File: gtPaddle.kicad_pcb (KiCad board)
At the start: 2 copper layers, 60.6 x 72.6 mm, 46 parts, among them IC1 74157N, IC2 74157N, J1 Conn_01x02_Pin, J2 Conn_01x02_Pin, J3 Conn_01x02_Pin, J4 Conn_01x02_Pin, Q1 2N3904, Q10 2N3904, Q2 2N3904, Q3 2N3904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

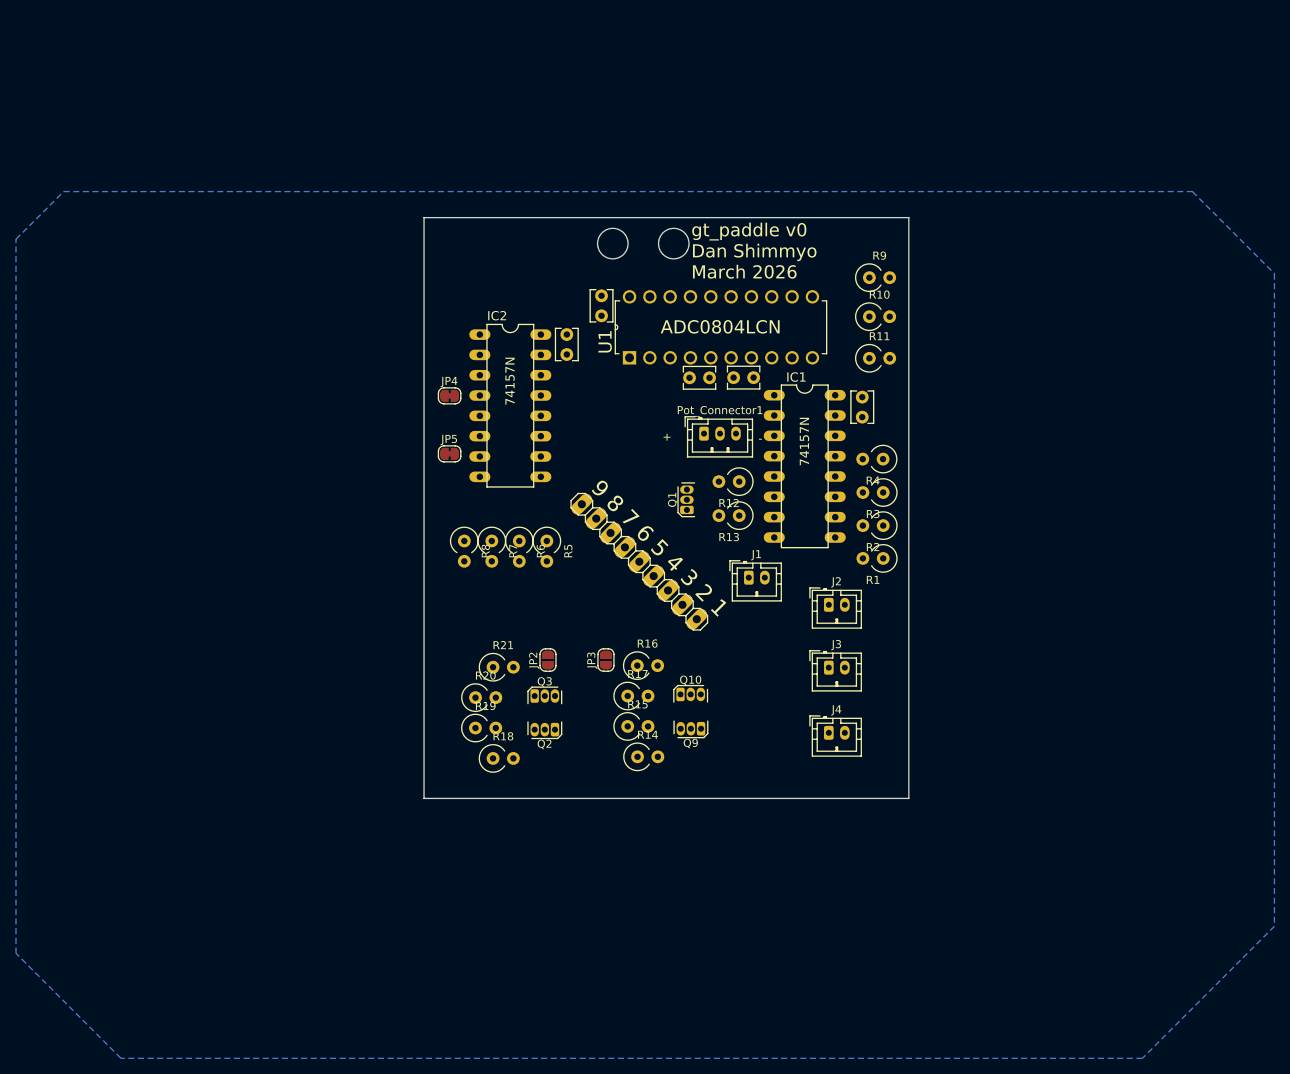
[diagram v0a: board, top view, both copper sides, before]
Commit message: more compact
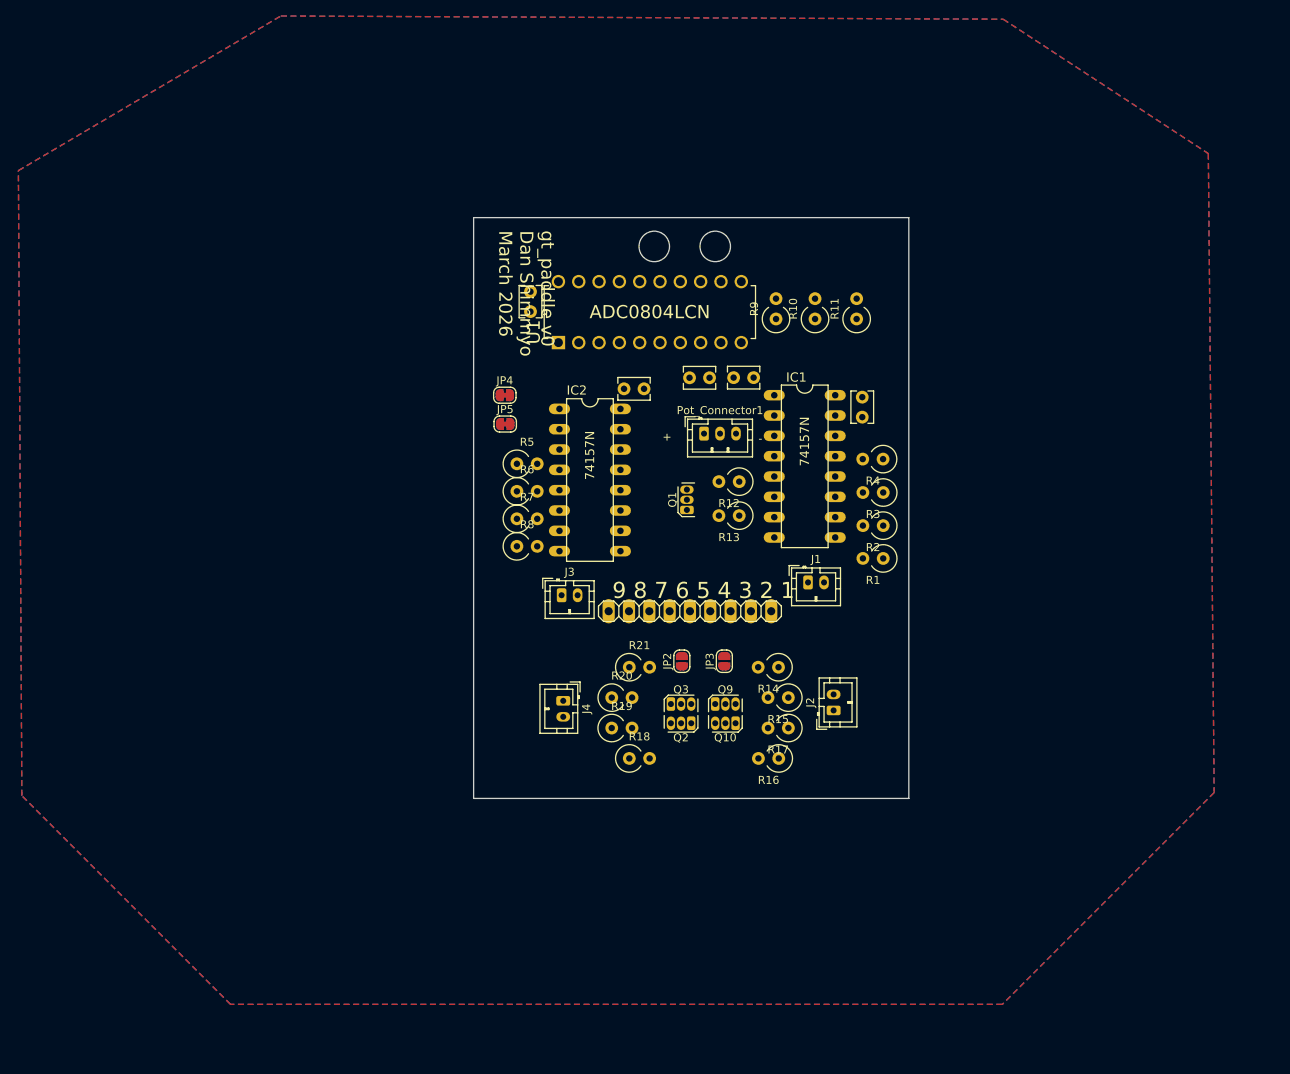
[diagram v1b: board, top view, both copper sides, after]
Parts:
- moved J3 34.6 mm to (133.4, 114.8)
- moved J4 33.4 mm to (133.6, 128.0), turned to -90 degrees
- moved R16 21.1 mm to (160.5, 135.2), turned to 180 degrees
- moved R14 20.9 mm to (160.5, 123.8), turned to 180 degrees
- moved R17 20.5 mm to (161.7, 131.4), turned to 180 degrees
- moved R15 20.4 mm to (161.7, 127.6), turned to 180 degrees
- moved Q3 17.1 mm to (147.1, 128.4)
- moved Q2 17.0 mm to (149.6, 130.8)
- moved R18 17.0 mm to (141.9, 135.2)
- moved R21 17.0 mm to (141.9, 123.8)
- moved R19 17.0 mm to (139.7, 131.4)
- moved R20 17.0 mm to (139.7, 127.6)
- moved JP2 16.7 mm to (148.4, 123.0)
- moved JP3 14.8 mm to (153.7, 123.0)
- moved IC2 13.6 mm to (136.9, 100.4)
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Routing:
- added copper zone on F.Cu, net GND
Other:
- board size 60.6 x 72.6 mm -> 54.4 x 72.6 mm

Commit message: started drawing traces
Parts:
- added ?: , , F.Cu at (129.7, 71.3)
- added ?: , , F.Cu at (135.6, 136.7)
- added ?: , , F.Cu at (172.4, 71.8)
- added ?: , , F.Cu at (165.4, 136.6)
- moved JP5 5.80 mm to (132.2, 93.3)
- moved JP4 5.80 mm to (132.1, 89.7)
- moved J4 4.60 mm to (133.8, 123.4)
- moved J2 4.50 mm to (167.4, 124.7)
- moved R5 4.26 mm to (132.0, 97.5), turned to 180 degrees
- moved R6 4.20 mm to (132.0, 101.4), turned to 180 degrees
- moved R8 4.19 mm to (132.0, 109.0), turned to 180 degrees
- moved R7 4.18 mm to (132.0, 105.2), turned to 180 degrees
- moved R4 2.74 mm to (171.3, 96.2), turned to 0 degrees
- moved R1 2.74 mm to (171.3, 108.7), turned to 0 degrees
- moved R3 2.74 mm to (171.3, 100.4), turned to 0 degrees
- moved R2 2.74 mm to (171.3, 104.6), turned to 0 degrees
- moved IC2 2.55 mm to (139.5, 100.5)
- moved C3 2.35 mm to (143.6, 89.0)
- moved Q10 1.22 mm to (155.3, 132.0)
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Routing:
- net VCC: track 0.00 -> 191.9 mm
- net Net-(Pot_Connector1-Pin_2): track 0.00 -> 18.7 mm
- net GND: vias 0 -> 6
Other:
- board size 54.4 x 72.6 mm -> 51.4 x 72.6 mm
- board text removed: "+"
- board text removed: "-"

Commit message: power routing
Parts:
- removed @HOLE4, @HOLE5: , 
- moved JP1 44.6 mm to (151.0, 72.2)
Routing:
- net Net-(Q1-C): track 0.00 -> 23.8 mm
- net VCC: track 191.9 -> 210.4 mm

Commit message: more trace work but not happy
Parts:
- moved R11 36.7 mm to (134.6, 71.6), turned to 0 degrees
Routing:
- net Net-(IC1A-4Y): track 0.00 -> 53.8 mm
- net Net-(JP3-B): track 0.00 -> 48.2 mm, vias 0 -> 1
- net Net-(JP2-B): track 0.00 -> 44.5 mm, vias 0 -> 1
- net Net-(IC1A-1Y): track 0.00 -> 31.6 mm, vias 0 -> 1
- net Net-(U1-CLK_IN): track 0.00 -> 24.3 mm, vias 0 -> 2
- net Net-(IC1A-2Y): track 0.00 -> 24.1 mm, vias 0 -> 1
- net Net-(U1-VREF/2): track 0.00 -> 14.0 mm
- net Net-(U1-CLK_R): track 0.00 -> 4.40 mm
- net GND: vias 6 -> 53

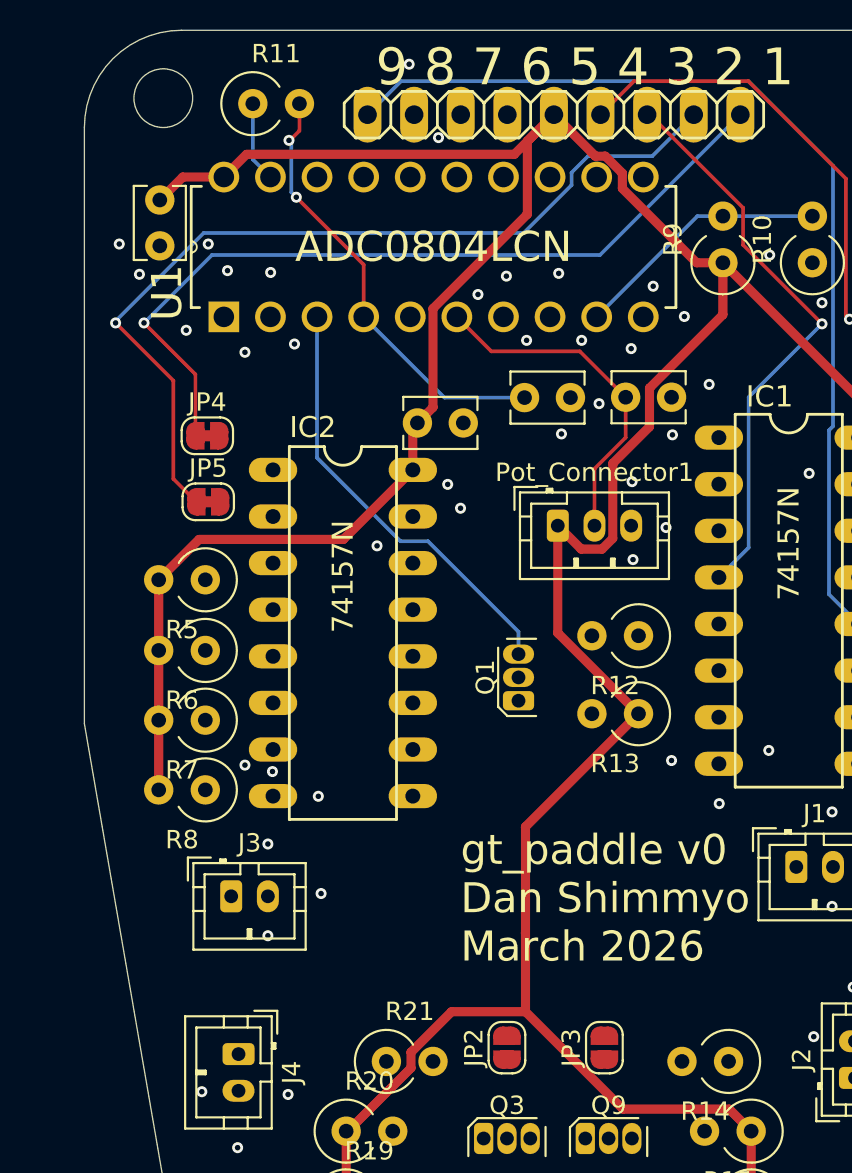
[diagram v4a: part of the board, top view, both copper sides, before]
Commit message: removed extra resistors from pcb layout
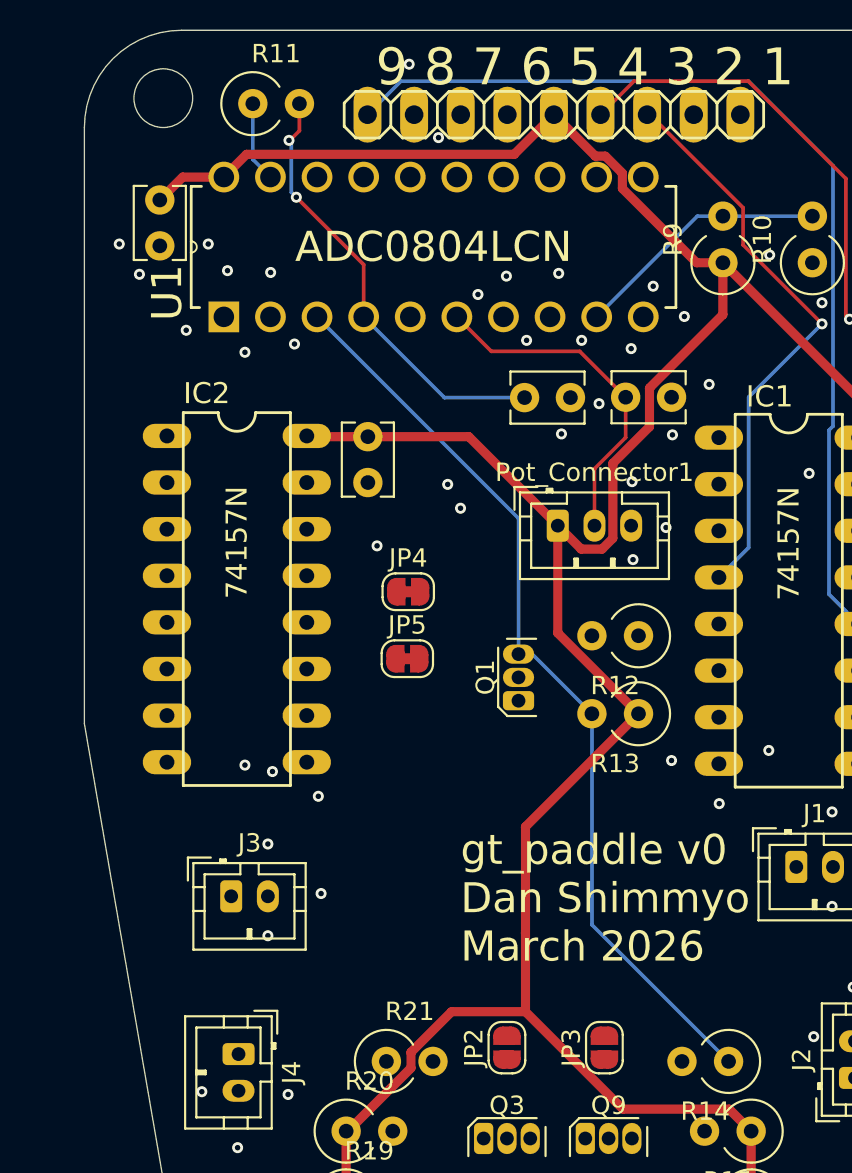
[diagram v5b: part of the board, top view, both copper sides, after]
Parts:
- removed R5, R6, R7, R8: 1k, Resistor_THT:R_Axial_DIN0309_L9.0mm_D3.2mm_P2.54mm_Vertical
- moved JP4 13.9 mm to (143.1, 98.2)
- moved JP5 13.8 mm to (143.0, 101.8)
- moved IC2 6.07 mm to (133.7, 98.6)
- moved C3 2.80 mm to (140.8, 89.8), turned to -90 degrees
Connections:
- IC2 pad 10: Net-(IC2A-3B) -> GND
- IC2 pad 11: Net-(IC2A-3A) -> GND
- IC2 pad 13: Net-(IC2A-4B) -> GND
- IC2 pad 14: Net-(IC2A-4A) -> GND
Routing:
- net Net-(JP3-B): track 48.2 -> 0.00 mm, vias 1 -> 0
- net Net-(JP2-B): track 44.5 -> 0.00 mm, vias 1 -> 0
- net VCC: track 210.4 -> 175.8 mm
- net Net-(Q1-C): track 23.8 -> 50.3 mm

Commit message: remove npn muxes
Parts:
- removed ? (x4): , 
- removed JP2, JP3: SolderJumper_2_Open, Jumper:SolderJumper-2_P1.3mm_Open_RoundedPad1.0x1.5mm
- removed JP4, JP5: SolderJumper_2_Bridged, Jumper:SolderJumper-2_P1.3mm_Bridged_RoundedPad1.0x1.5mm
- removed Q10, Q2, Q3, Q9: 2N3904, Package_TO_SOT_THT:TO-92S-EBC
- removed R14, R16, R18, R21: 10K, Resistor_THT:R_Axial_DIN0309_L9.0mm_D3.2mm_P2.54mm_Vertical
- removed R15, R17, R19, R20: 3.3K, Resistor_THT:R_Axial_DIN0309_L9.0mm_D3.2mm_P2.54mm_Vertical
- moved R4 45.8 mm to (136.7, 126.2), turned to 90 degrees
- moved C5 45.1 mm to (165.6, 103.9), turned to 90 degrees
- moved R11 39.3 mm to (166.7, 94.2), turned to 180 degrees
- moved R3 36.0 mm to (146.1, 126.1), turned to 90 degrees
- moved J1 34.9 mm to (135.7, 133.2)
- moved J4 33.3 mm to (165.6, 133.3), turned to 0 degrees
- moved U1 33.2 mm to (138.8, 104.0), turned to -90 degrees
- moved J3 28.8 mm to (155.5, 133.2)
- moved R13 28.6 mm to (158.6, 76.4), turned to -90 degrees
- moved R2 26.2 mm to (156.2, 126.0), turned to 90 degrees
- moved Q1 25.4 mm to (151.8, 78.8), turned to 0 degrees
- moved C4 25.0 mm to (154.4, 108.8), turned to 0 degrees
- moved R12 24.0 mm to (146.0, 78.7), turned to 0 degrees
- moved J2 23.8 mm to (145.2, 133.3), turned to 0 degrees
- moved C3 20.6 mm to (131.9, 108.3), turned to 0 degrees
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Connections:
- JP1 pad 1: Net-(JP2-B) -> Net-(IC2A-1Y)
- JP1 pad 2: Net-(JP3-B) -> Net-(IC2A-2Y)
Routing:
- net VCC: track 175.8 -> 0.00 mm
- net Net-(IC1A-4Y): track 53.8 -> 0.00 mm
- net Net-(Q1-C): track 50.3 -> 0.00 mm
- net Net-(IC1A-1Y): track 31.6 -> 0.00 mm, vias 1 -> 0
- net Net-(U1-CLK_IN): track 24.3 -> 0.00 mm, vias 2 -> 0
- net Net-(IC1A-2Y): track 24.1 -> 0.00 mm, vias 1 -> 0
- net Net-(Pot_Connector1-Pin_2): track 18.7 -> 0.00 mm
- net Net-(U1-VREF/2): track 14.0 -> 0.00 mm
- net Net-(U1-CLK_R): track 4.40 -> 0.00 mm
- net GND: vias 53 -> 1

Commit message: layout tweaks
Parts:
- added ?: , , F.Cu at (130.7, 72.9)
- added ?: , , F.Cu at (171.5, 72.9)
- added ?: , , F.Cu at (171.5, 100.6)
- added ?: , , F.Cu at (130.7, 100.6)
- moved R10 32.1 mm to (133.8, 89.1), turned to -90 degrees
- moved R9 29.0 mm to (139.4, 89.1)
- moved R12 18.5 mm to (161.2, 89.1), turned to -90 degrees
- moved R13 15.4 mm to (167.3, 89.1)
- moved Q1 10.5 mm to (162.0, 81.5)
- moved Pot_Connector1 5.25 mm to (148.8, 81.8)
- moved R11 3.76 mm to (170.4, 95.0)
- moved IC1 1.05 mm to (162.1, 115.5)
- moved C4 1.05 mm to (153.4, 108.8)
- moved JP1 0.17 mm to (150.8, 72.2)
- moved C1 0.11 mm to (153.6, 93.8)
- moved C2 0.11 mm to (146.3, 93.8)
- moved C5 0.11 mm to (165.6, 103.8)
- moved U1 0.11 mm to (138.8, 103.9)
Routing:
- net GND: vias 1 -> 0
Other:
- board text added: "1 2 3 4 5 6 7 8 9"

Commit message: eliminated errors
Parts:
- moved Q1 11.5 mm to (155.7, 91.2)
- moved R1 5.04 mm to (161.2, 126.0)
- moved J4 4.84 mm to (161.2, 131.2)
- moved J1 3.89 mm to (139.0, 131.2)
- moved R4 2.88 mm to (139.5, 126.0)
- moved J3 2.51 mm to (154.0, 131.2)
- moved J2 2.49 mm to (146.6, 131.2)
- moved R2 1.93 mm to (154.2, 126.0)
- moved C4 1.57 mm to (153.1, 107.2)
- moved IC1 1.57 mm to (161.8, 113.9)
- moved C3 1.57 mm to (131.7, 106.8)
- moved IC2 1.57 mm to (140.5, 113.9)
- moved R3 0.12 mm to (146.1, 126.0)
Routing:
- net VCC: track 0.00 -> 170.1 mm
- net Net-(IC1A-~{A}/B): track 0.00 -> 102.8 mm, vias 0 -> 1
- net Net-(IC2A-2Y): track 0.00 -> 76.8 mm, vias 0 -> 1
- net Net-(IC1A-1Y): track 0.00 -> 69.8 mm, vias 0 -> 1
- net Net-(IC1A-4Y): track 0.00 -> 67.9 mm, vias 0 -> 4
- net Net-(IC2A-1Y): track 0.00 -> 64.2 mm, vias 0 -> 3
- net Net-(IC1A-2Y): track 0.00 -> 55.9 mm
- net Net-(IC1A-2A): track 0.00 -> 49.2 mm
- net Net-(IC1A-3Y): track 0.00 -> 47.5 mm
- net Net-(IC1A-1A): track 0.00 -> 42.4 mm
- net Net-(IC1A-3A): track 0.00 -> 39.3 mm, vias 0 -> 1
- net Net-(IC1A-3B): track 0.00 -> 38.5 mm
- net Net-(IC1A-4A): track 0.00 -> 37.5 mm
- net Net-(IC1A-2B): track 0.00 -> 30.7 mm
- net Net-(U1-CLK_R): track 0.00 -> 28.5 mm, vias 0 -> 3
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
